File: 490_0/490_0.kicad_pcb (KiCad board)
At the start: 4 copper layers, 211.8 x 143.2 mm, 193 parts, among them J1 PAD, J10 PAD, J11 S3B-XH-A, J12 2000-1-1-20-00-BK, J13 S2B-ZR, J14 2000-1-1-20-00-BK, J15 S3B-XH-A, J16 DF40HC(3.0)-100DS-0.4V(58), J17 DF40HC(3.0)-100DS-0.4V(58), J18 TS-103-G-A, J2 PAD, J20 YO0201500000G, J21 TS-102-G-A, J22 2000-1-1-20-00-BK, J23 S3B-XH-A, J3 PAD, J4 PAD, J5 PAD, J6 PAD, J7 629105150521, J8 0526101571, J9 PAD, Q1 AO3400A, Q2 AO3400A, Q3 AO3400A, Q4 AO3400A, Q5 AO3400A, Q6 BSS84, SW1 TL2230EEF140, SW2 TL1105LF160Q, SW3 TL1105LF160Q, SW4 TL1105LF160Q, SW5 TL1105LF160Q, SW6 TL1105LF160Q, SW7 TL1105LF160Q, SW8 TL1105LF160Q, U1 MAX98357A, U10 EMI8142MUTAG, U11 SP3003-02XTG, U12 TPD8S009DSMR, U13 SP3003-02XTG, U14 SP3003-02XTG, U15 SP3003-02XTG, U16 SP3003-02XTG, U17 SP3003-02XTG, U18 TPD8S009DSMR, U19 SP3003-02XTG, U2 TPS2553DBVR, U3 TPS2553DBVR, U4 USB2512B-I/M2, U5 TS3USB221AQRSERQ1, U6 PCA9685, U7 TPS566247DRLR, U8 MP2639AGR-Z, U9 EMI8142MUTAG, Y1 24M20P2/XT324-10/10

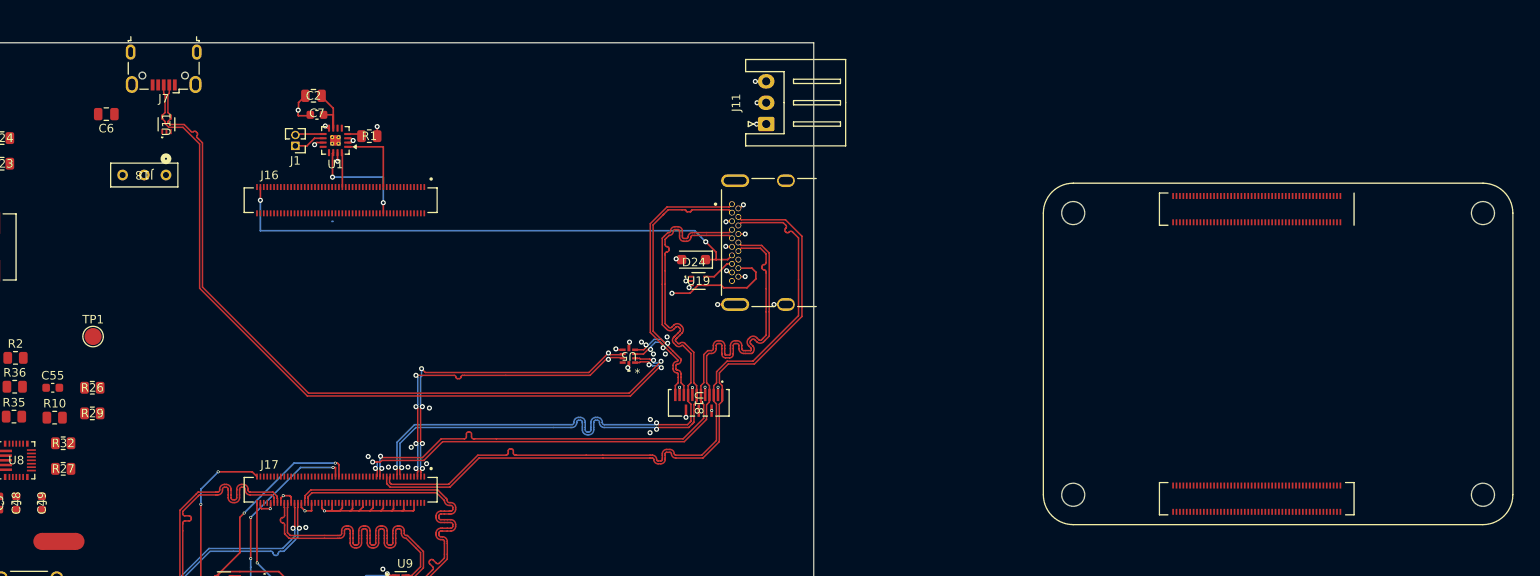
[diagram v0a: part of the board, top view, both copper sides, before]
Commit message: Connected microUSB port
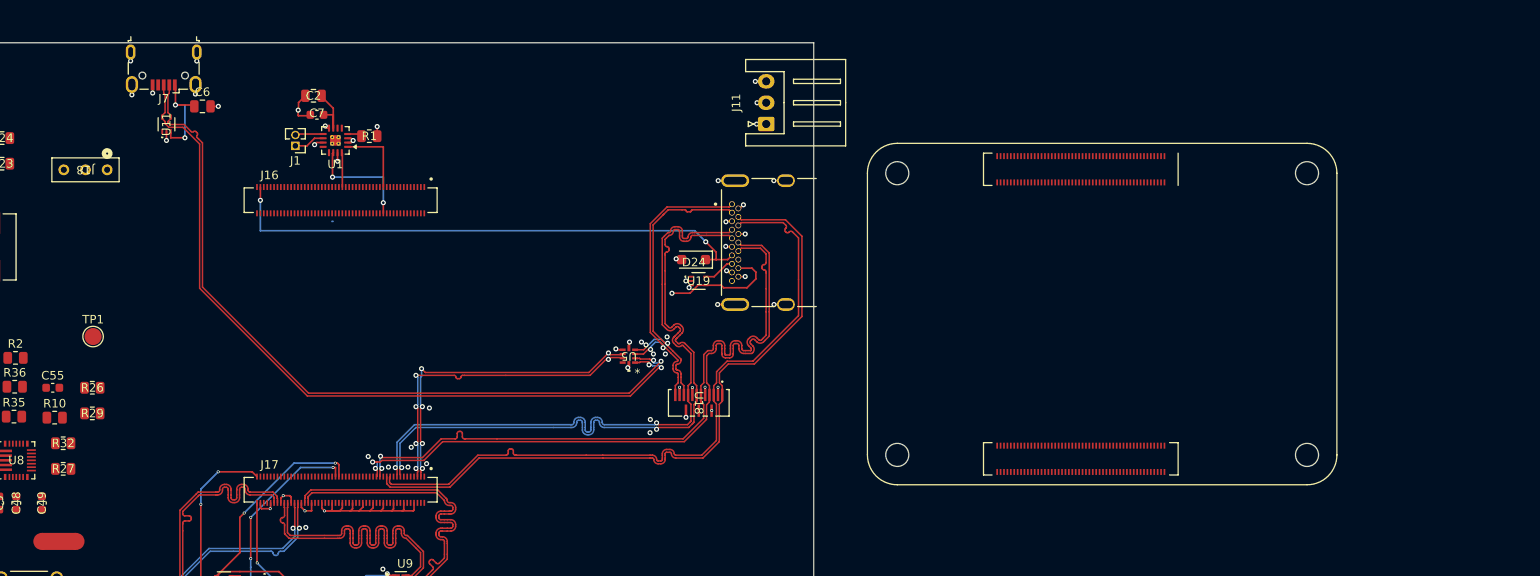
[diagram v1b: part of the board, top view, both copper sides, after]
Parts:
- moved ? 21.1 mm to (235.2, 96.1)
- moved C6 11.3 mm to (103.3, 90.7), turned to 0 degrees
- moved J18 6.92 mm to (89.6, 98.1)
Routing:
- net VBUS_5V: track 0.00 -> 12.0 mm, vias 0 -> 2
- net GND: track 70.5 -> 80.8 mm, vias 49 -> 58

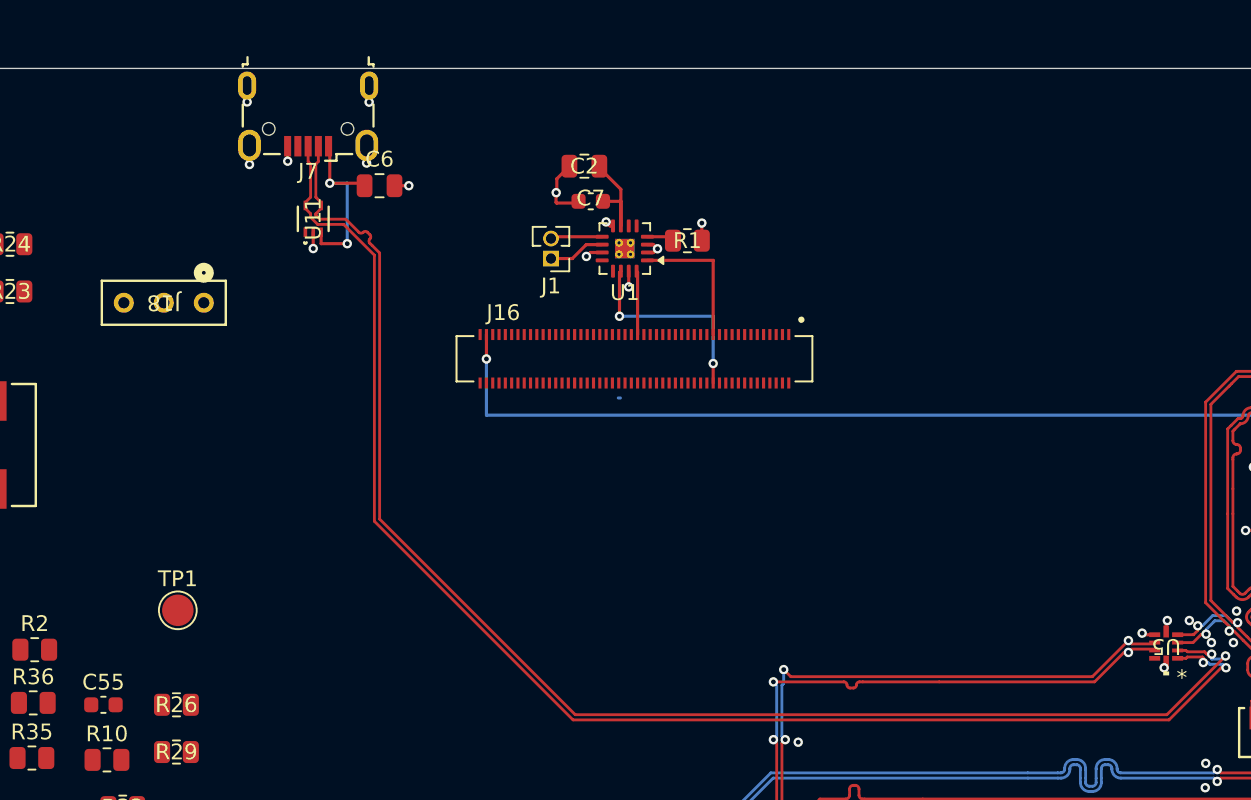
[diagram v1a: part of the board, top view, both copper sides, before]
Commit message: Routed j18
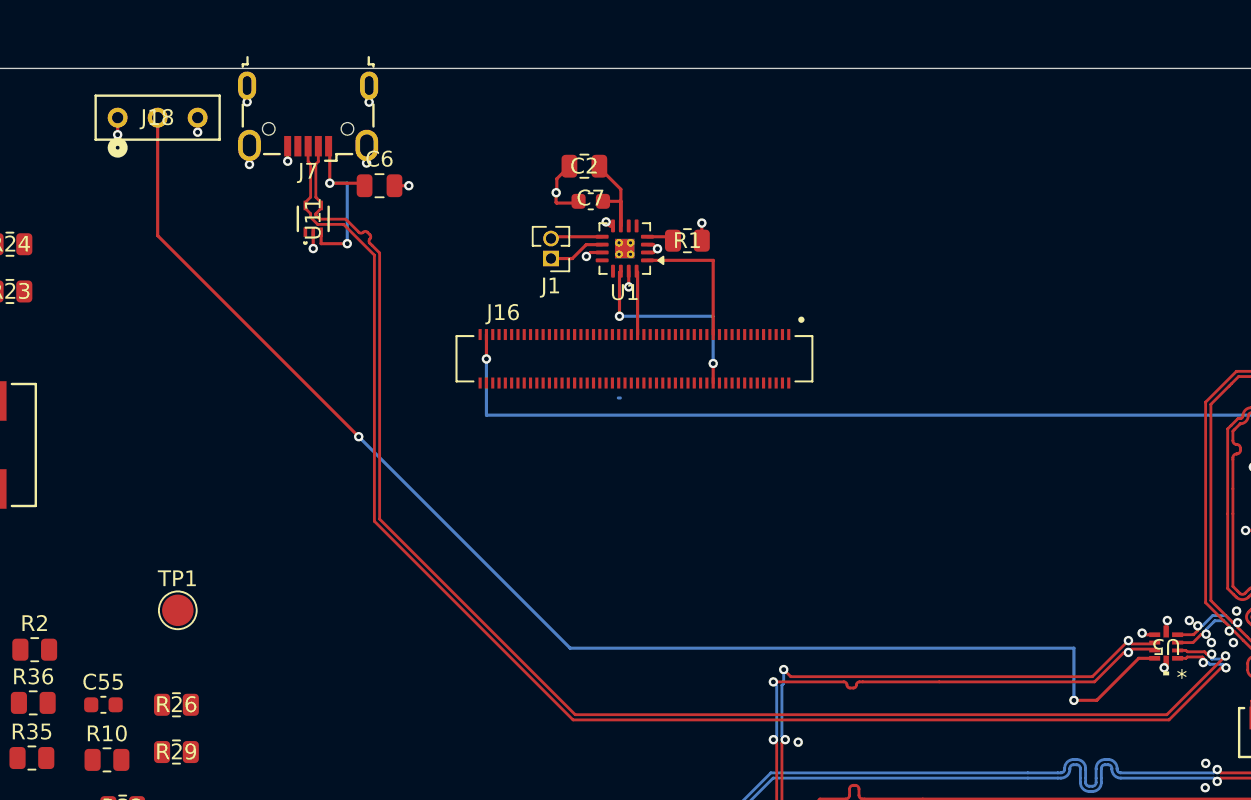
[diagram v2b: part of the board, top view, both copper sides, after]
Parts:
- moved J18 11.8 mm to (89.2, 86.4), turned to 0 degrees
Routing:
- net Net-(J18-Pin_2): track 0.00 -> 86.1 mm, vias 0 -> 2
- net +3.3V: track 3.52 -> 4.60 mm, vias 6 -> 7
- net GND: track 80.8 -> 81.8 mm, vias 58 -> 59
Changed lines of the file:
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@@
 	(footprint "*CapStone*:CON3_1X3_TU_HTS_SAI - 3POS Connector"
 		(layer "F.Cu")
-		(at 89.61 98.1424 180)
+		(at 89.22 86.3876)
 		(tags "TS-103-G-A ")
 		(property "Reference" "J18"
-			(at 0 0 180)
+			(at 0 0 0)
 			(unlocked yes)
 			(layer "F.SilkS")
@@
 		)
 		(property "Value" "TS-103-G-A"
-			(at 0 0 180)
+			(at 0 0 0)
 			(unlocked yes)
 			(layer "F.Fab")
@@
 		)
 		(property "Specifications" "HEADER 1x3 MALE PINS 0.100” 180deg"
-			(at 0 0 180)
+			(at 0 0 0)
 			(unlocked yes)
 			(layer "F.Fab")
@@
 		)
 		(property "Manufacturer" "Samtec Inc."
-			(at 0 0 180)
+			(at 0 0 0)
 			(unlocked yes)
 			(layer "F.Fab")
@@
 		)
 		(property "Part Number" "1-0301FBV0T"
-			(at 0 0 180)
+			(at 0 0 0)
 			(unlocked yes)
 			(layer "F.Fab")
@@
 		)
 		(property "Digikey Link" "https://www.digikey.ca/en/products/detail/samtec-inc/TS-103-G-A/1105459"
-			(at 0 0 180)
+			(at 0 0 0)
 			(unlocked yes)
 			(layer "F.Fab")
@@
 		)
 		(property "Manufacturer Part" "TS-103-G-A"
-			(at 0 0 180)
+			(at 0 0 0)
 			(unlocked yes)
 			(layer "F.Fab")
@@
 		)
 		(property "Price" "1.27"
-			(at 0 0 180)
+			(at 0 0 0)
 			(unlocked yes)
 			(layer "F.Fab")
@@
 		)
 		(property "Supplier" "DigiKey"
-			(at 0 0 180)
+			(at 0 0 0)
 			(unlocked yes)
 			(layer "F.Fab")
@@
 		)
 		(property "Supplier P/N" "SAM1111-03-ND"
-			(at 0 0 180)
+			(at 0 0 0)
 			(unlocked yes)
 			(layer "F.Fab")
@@
 		)
 		(property "Type" "Through Hole"
-			(at 0 0 180)
+			(at 0 0 0)
 			(unlocked yes)
 			(layer "F.Fab")
@@
 		)
 		(property "Unit" "pcs"
-			(at 0 0 180)
+			(at 0 0 0)
 			(unlocked yes)
 			(layer "F.Fab")
@@
 		(attr through_hole)
 		(fp_line
-			(start 3.937 1.397)
-			(end 3.937 -1.397)
+			(start -3.937 -1.397)
+			(end -3.937 1.397)
 			(stroke
 				(width 0.1524)
@@
 		)
 		(fp_line
-			(start 3.937 -1.397)
-			(end -3.937 -1.397)
+			(start -3.937 1.397)
+			(end 3.937 1.397)
 			(stroke
 				(width 0.1524)
@@
 		)
 		(fp_line
-			(start -3.937 1.397)
-			(end 3.937 1.397)
+			(start 3.937 -1.397)
+			(end -3.937 -1.397)
 			(stroke
 				(width 0.1524)
@@
 		)
 		(fp_line
-			(start -3.937 -1.397)
-			(end -3.937 1.397)
+			(start 3.937 1.397)
+			(end 3.937 -1.397)
 			(stroke
 				(width 0.1524)
@@
 		)
 		(fp_line
-			(start 4.064 1.524)
-			(end 4.064 -1.524)
+			(start -4.064 -1.524)
+			(end -4.064 1.524)
 			(stroke
 				(width 0.1524)
@@
 		)
 		(fp_line
-			(start 4.064 -1.524)
-			(end 3.429 -1.524)
+			(start -4.064 1.524)
+			(end -3.429 1.524)
 			(stroke
 				(width 0.1524)
@@
 		)
 		(fp_line
-			(start 3.429 2.159)
-			(end 3.429 1.524)
+			(start -3.429 -2.159)
+			(end -3.429 -1.524)
 			(stroke
 				(width 0.1524)
@@
 		)
 		(fp_line
-			(start 3.429 1.524)
-			(end 4.064 1.524)
+			(start -3.429 -1.524)
+			(end -4.064 -1.524)
 			(stroke
 				(width 0.1524)
@@
 		)
 		(fp_line
-			(start 3.429 -1.524)
-			(end 3.429 -2.159)
+			(start -3.429 1.524)
+			(end -3.429 2.159)
 			(stroke
 				(width 0.1524)
@@
 		)
 		(fp_line
-			(start 3.429 -2.159)
-			(end -3.429 -2.159)
+			(start -3.429 2.159)
+			(end 3.429 2.159)
 			(stroke
 				(width 0.1524)
@@
 		)
 		(fp_line
-			(start -3.429 2.159)
-			(end 3.429 2.159)
+			(start 3.429 -2.159)
+			(end -3.429 -2.159)
 			(stroke
 				(width 0.1524)
@@
 		)
 		(fp_line
-			(start -3.429 1.524)
-			(end -3.429 2.159)
+			(start 3.429 -1.524)
+			(end 3.429 -2.159)
 			(stroke
 				(width 0.1524)
@@
 		)
 		(fp_line
-			(start -3.429 -1.524)
-			(end -4.064 -1.524)
+			(start 3.429 1.524)
+			(end 4.064 1.524)
 			(stroke
 				(width 0.1524)
@@
 		)
 		(fp_line
-			(start -3.429 -2.159)
-			(end -3.429 -1.524)
+			(start 3.429 2.159)
+			(end 3.429 1.524)
 			(stroke
 				(width 0.1524)
@@
 		)
 		(fp_line
-			(start -4.064 1.524)
-			(end -3.429 1.524)
+			(start 4.064 -1.524)
+			(end 3.429 -1.524)
 			(stroke
 				(width 0.1524)
@@
 		)
 		(fp_line
-			(start -4.064 -1.524)
-			(end -4.064 1.524)
+			(start 4.064 1.524)
+			(end 4.064 -1.524)
 			(stroke
 				(width 0.1524)
@@
 		)
 		(fp_line
-			(start 3.81 1.27)
-			(end 3.81 -1.27)
+			(start -3.81 -1.27)
+			(end -3.81 1.27)
 			(stroke
 				(width 0.0254)
@@
 		)
 		(fp_line
-			(start 3.81 -1.27)
-			(end -3.81 -1.27)
+			(start -3.81 1.27)
+			(end 3.81 1.27)
 			(stroke
 				(width 0.0254)
@@
 		)
 		(fp_line
-			(start -3.81 1.27)
-			(end 3.81 1.27)
+			(start 3.81 -1.27)
+			(end -3.81 -1.27)
 			(stroke
 				(width 0.0254)
@@
 		)
 		(fp_line
-			(start -3.81 -1.27)
-			(end -3.81 1.27)
+			(start 3.81 1.27)
+			(end 3.81 -1.27)
 			(stroke
 				(width 0.0254)
@@
 		)
 		(fp_text user "${REFERENCE}"
-			(at 0 0 180)
+			(at 0 0 0)
 			(unlocked yes)
 			(layer "F.Fab")
@@
 		)
 		(pad "1" thru_hole circle
-			(at -2.54 0 270)
+			(at -2.54 0 90)
 			(size 1.27 1.27)
 			(drill 0.7112)
@@
 		)
 		(pad "2" thru_hole circle
-			(at 0 0 270)
+			(at 0 0 90)
 			(size 1.27 1.27)
 			(drill 0.7112)
@@
 		)
 		(pad "3" thru_hole circle
-			(at 2.54 0 270)
+			(at 2.54 0 90)
 			(size 1.27 1.27)
 			(drill 0.7112)
@@
 	)
 	(segment
+		(start 91.76 86.3876)
+		(end 91.76 87.31)
+		(width 0.2)
+		(layer "F.Cu")
+		(net 2)
+	)
+	(segment
 		(start 160.575434 111.162767)
 		(end 159.952611 111.162768)
@@
 	)
 	(via
+		(at 91.76 87.31)
+		(size 0.6)
+		(drill 0.3)
+		(layers "F.Cu" "B.Cu")
+		(net 2)
+	)
+	(via
 		(at 106.426 153.336)
 		(size 0.6)
@@
 	)
 	(segment
+		(start 86.68 86.3876)
+		(end 86.68 87.47)
+		(width 0.2)
+		(layer "F.Cu")
+		(net 3)
+	)
+	(segment
 		(start 166.093056 110.663666)
 		(end 166.874849 110.663666)
@@
 	)
 	(via
+		(at 86.68 87.47)
+		(size 0.6)
+		(drill 0.3)
+		(layers "F.Cu" "B.Cu")
+		(net 3)
+	)
+	(via
 		(at 153.141245 121.324011)
 		(size 0.6)
@@
 	)
 	(segment
+		(start 89.22 86.3876)
+		(end 89.22 93.88)
+		(width 0.2)
+		(layer "F.Cu")
+		(net 247)
+	)
+	(segment
+		(start 89.22 93.88)
+		(end 101.99 106.65)
+		(width 0.2)
+		(layer "F.Cu")
+		(net 247)
+	)
+	(segment
+		(start 148.86 123.39)
+		(end 151.525988 120.724012)
+		(width 0.2)
+		(layer "F.Cu")
+		(net 247)
+	)
+	(segment
+		(start 147.41 123.39)
+		(end 148.86 123.39)
+		(width 0.2)
+		(layer "F.Cu")
+		(net 247)
+	)
+	(segment
+		(start 151.525988 120.724012)
+		(end 152.541245 120.724012)
+		(width 0.2)
+		(layer "F.Cu")
+		(net 247)
+	)
+	(via
+		(at 101.99 106.65)
+		(size 0.6)
+		(drill 0.3)
+		(layers "F.Cu" "B.Cu")
+		(net 247)
+	)
+	(via
+		(at 147.41 123.39)
+		(size 0.6)
+		(drill 0.3)
+		(layers "F.Cu" "B.Cu")
+		(net 247)
+	)
+	(segment
+		(start 147.41 120.08)
+		(end 147.41 123.39)
+		(width 0.2)
+		(layer "B.Cu")
+		(net 247)
+	)
+	(segment
+		(start 101.99 106.65)
+		(end 115.42 120.08)
+		(width 0.2)
+		(layer "B.Cu")
+		(net 247)
+	)
+	(segment
+		(start 115.42 120.08)
+		(end 147.41 120.08)
+		(width 0.2)
+		(layer "B.Cu")
+		(net 247)
+	)
+	(segment

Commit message: Changed pin assignment for the buttons on PCB1 in the schematic
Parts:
- moved C30 316.0 mm to (159.8, 93.7), turned to 180 degrees
- moved SW6 311.9 mm to (160.6, 86.9)
- moved C29 303.4 mm to (147.4, 93.7), turned to 180 degrees
- moved SW2 294.4 mm to (135.2, 86.9)
- moved C28 285.3 mm to (129.5, 93.7)
- moved SW4 277.9 mm to (147.8, 87.0)
- moved C25 262.5 mm to (98.5, 57.8)
- moved C26 262.5 mm to (98.5, 60.3)
- moved C27 262.5 mm to (98.5, 62.8)
- moved R37 262.5 mm to (107.1, 63.8)
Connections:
- SW2 pad 1: GND -> (no net)
- SW2 pad 3: (no net) -> GND
- SW3 pad 1: GND -> (no net)
- SW3 pad 2: Net-(C27--) -> GND
- SW3 pad 3: (no net) -> Net-(C27--)
- SW4 pad 1: GND -> (no net)
- SW4 pad 3: (no net) -> GND
- SW5 pad 1: GND -> (no net)
- SW5 pad 2: Net-(C26--) -> GND
- SW5 pad 3: (no net) -> Net-(C26--)
- SW6 pad 1: GND -> (no net)
- SW6 pad 3: (no net) -> GND
- SW7 pad 1: GND -> (no net)
- SW7 pad 2: Net-(C25--) -> GND
- SW7 pad 3: (no net) -> Net-(C25--)
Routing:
- net Net-(C30--): track 0.00 -> 49.8 mm
- net Net-(C29--): track 0.00 -> 40.1 mm
- net Net-(C28--): track 0.00 -> 25.5 mm
- net GND: track 81.8 -> 84.7 mm, vias 59 -> 62

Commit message: Routed buttons
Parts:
- moved SW5 238.0 mm to (64.7, 87.1), turned to 180 degrees
- moved SW7 222.5 mm to (77.4, 87.1), turned to 180 degrees
- moved SW3 202.9 mm to (52.0, 87.0), turned to 180 degrees
- moved C42 76.4 mm to (57.6, 60.5)
- moved C43 76.4 mm to (40.5, 62.0)
- moved C44 76.4 mm to (36.6, 62.0)
- moved C46 76.4 mm to (57.1, 54.5)
- moved C48 76.4 mm to (61.1, 63.5)
- moved C49 76.4 mm to (64.2, 63.5)
- moved C5 76.4 mm to (59.1, 63.5)
- moved D10 76.4 mm to (46.6, 61.5)
- moved J15 76.4 mm to (30.6, 55.5)
- moved L2 76.4 mm to (53.1, 62.0)
- moved NT1 76.4 mm to (66.2, 68.0)
- moved R27 76.4 mm to (66.7, 59.5)
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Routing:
- net Net-(C27--): track 0.00 -> 97.0 mm, vias 0 -> 2
- net Net-(C26--): track 0.00 -> 82.4 mm, vias 0 -> 2
- net Net-(C25--): track 0.00 -> 67.8 mm, vias 0 -> 2
- net /PCB1/PCB1-Board Connector A/SDA1: track 13.8 -> 63.4 mm, vias 1 -> 2
- net /PCB1/PCB1-Board Connector A/SCL1: track 3.82 -> 52.4 mm, vias 0 -> 2
- net GND: track 84.7 -> 87.6 mm, vias 62 -> 65
